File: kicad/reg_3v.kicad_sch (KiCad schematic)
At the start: 7 parts

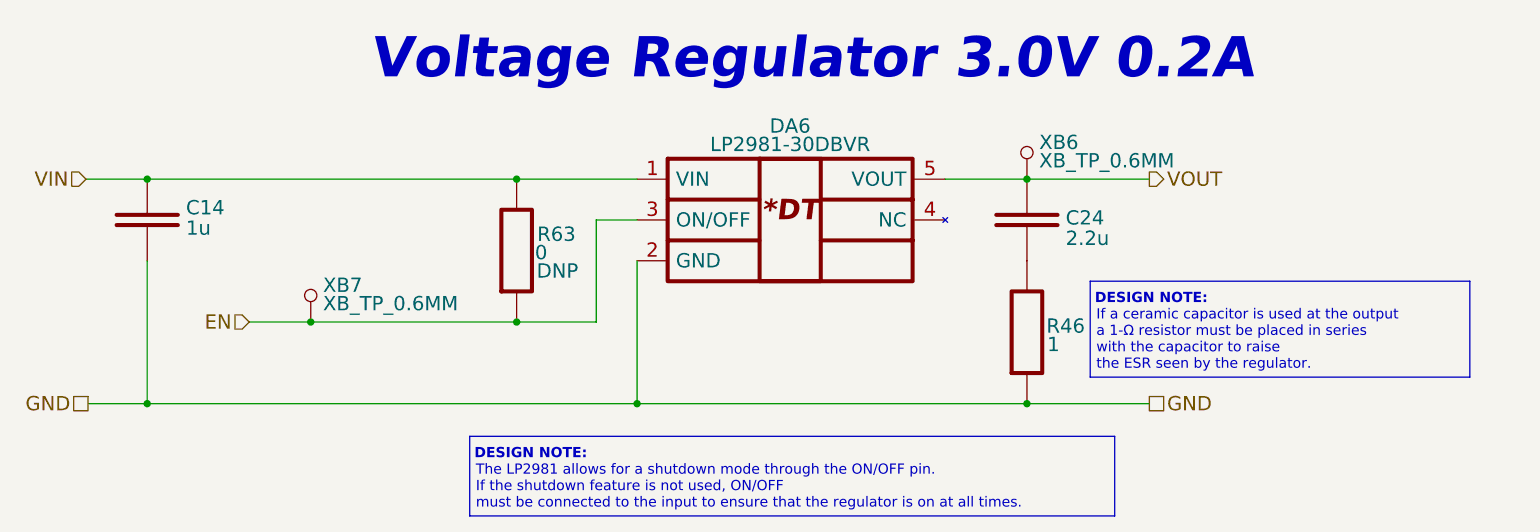
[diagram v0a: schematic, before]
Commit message: Reannotate schematic; Fix 5032 crystal footprint field; Update PCB with 5032 crystal
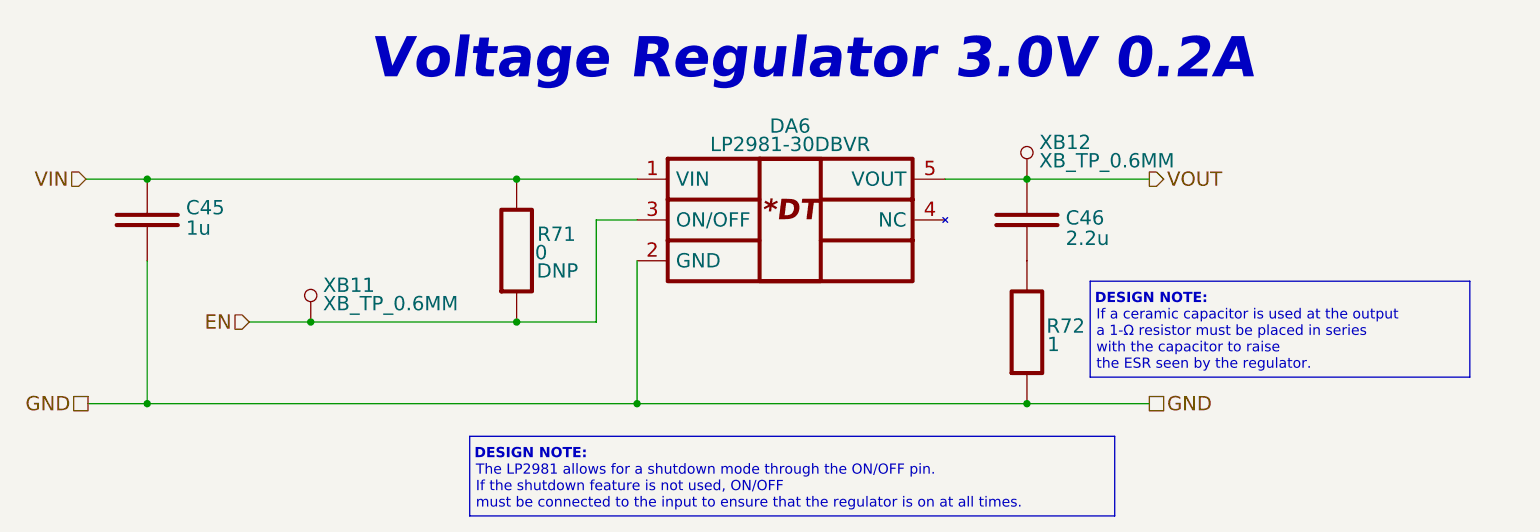
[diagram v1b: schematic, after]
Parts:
- renumbered C14 to C45, C24 to C46, R63 to R71, R46 to R72, XB7 to XB11, XB6 to XB12
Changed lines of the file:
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@@
   (symbol (lib_id "Capacitors:C_CAP") (at 183.642 85.598 270) (mirror x) (unit 1)
     (in_bom yes) (on_board yes)
-    (property "Reference" "C24" (id 0) (at 188.468 85.344 90)
+    (property "Reference" "C46" (id 0) (at 188.468 85.344 90)
       (effects (font (size 1.778 1.778)) (justify left))
     )
@@
   (symbol (lib_id "Capacitors:C_CAP") (at 74.168 85.598 270) (unit 1)
     (in_bom yes) (on_board yes)
-    (property "Reference" "C14" (id 0) (at 78.994 84.074 90)
+    (property "Reference" "C45" (id 0) (at 78.994 84.074 90)
       (effects (font (size 1.778 1.778)) (justify left))
     )
@@
   (symbol (lib_id "Connectors:XB_TP_0.6MM") (at 94.5147 98.298 0) (unit 1)
     (in_bom no) (on_board yes)
-    (property "Reference" "XB7" (id 0) (at 96.0387 93.726 0)
+    (property "Reference" "XB11" (id 0) (at 96.0387 93.726 0)
       (effects (font (size 1.778 1.778)) (justify left))
     )
@@
   (symbol (lib_id "Connectors:XB_TP_0.6MM") (at 183.642 80.518 0) (unit 1)
     (in_bom no) (on_board yes)
-    (property "Reference" "XB6" (id 0) (at 185.166 75.946 0)
+    (property "Reference" "XB12" (id 0) (at 185.166 75.946 0)
       (effects (font (size 1.778 1.778)) (justify left))
     )
@@
   (symbol (lib_id "Resistors:R_RES") (at 183.642 99.568 90) (unit 1)
     (in_bom yes) (on_board yes)
-    (property "Reference" "R46" (id 0) (at 188.468 98.806 90)
+    (property "Reference" "R72" (id 0) (at 188.468 98.806 90)
       (effects (font (size 1.778 1.778)))
     )
@@
   (symbol (lib_id "Resistors:R_RES") (at 120.142 89.408 90) (unit 1)
     (in_bom yes) (on_board yes)
-    (property "Reference" "R63" (id 0) (at 125.095 87.376 90)
+    (property "Reference" "R71" (id 0) (at 125.095 87.376 90)
       (effects (font (size 1.778 1.778)))
     )

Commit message: Add voltage value to caps, update BOM, SCH, ASM
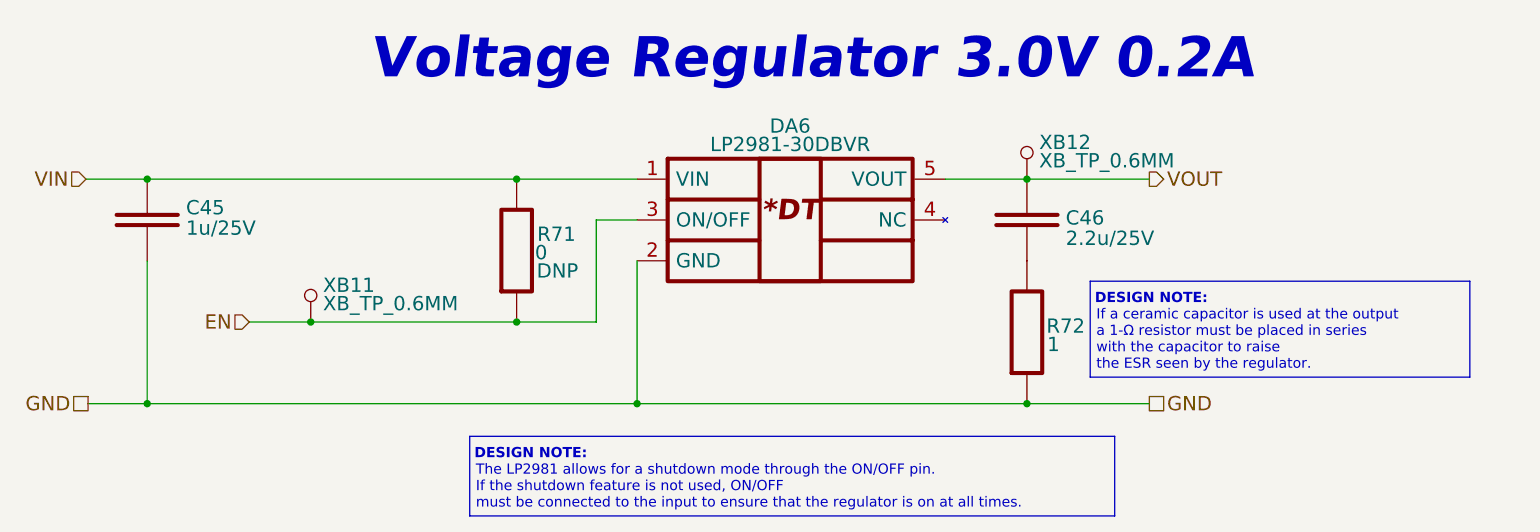
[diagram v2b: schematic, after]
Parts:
- C45: value 1u -> 1u/25V; Case/Package (none) -> 0603; Tolerance (none) -> ±10%; Type (none) -> X7R
- C46: value 2.2u -> 2.2u/25V; Case/Package (none) -> 0603; Tolerance (none) -> ±10%; Type (none) -> X7R
- R71: Case/Package 0000 -> 0603; Tolerance ±% -> ±5%
- R72: Tolerance ±% -> ±5%
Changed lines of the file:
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@@
     (effects (font (size 1.778 1.778)) (justify left))
   )
-  (symbol (lib_id "Capacitors:C_CAP") (at 183.642 85.598 270) (mirror x) (unit 1)
+  (symbol (lib_name "C_CAP_1") (lib_id "Capacitors:C_CAP") (at 183.642 85.598 270) (mirror x) (unit 1)
     (in_bom yes) (on_board yes)
     (property "Reference" "C46" (id 0) (at 188.468 85.344 90)
       (effects (font (size 1.778 1.778)) (justify left))
     )
-    (property "Value" "2.2u" (id 1) (at 188.468 87.884 90)
+    (property "Value" "2.2u/25V" (id 1) (at 188.468 87.884 90)
       (effects (font (size 1.778 1.778)) (justify left))
     )
@@
       (effects (font (size 1.778 1.778)))
     )
+    (property "Voltage" "" (id 5) (at 183.642 85.598 0)
+      (effects (font (size 1.27 1.27)) hide)
+    )
+    (property "Case/Package" "0603" (id 6) (at 183.642 85.598 0)
+      (effects (font (size 1.27 1.27)) hide)
+    )
+    (property "Type" "X7R" (id 7) (at 173.482 85.598 0)
+      (effects (font (size 1.27 1.27)) hide)
+    )
+    (property "Tolerance" "±10%" (id 8) (at 170.942 85.598 0)
+      (effects (font (size 1.27 1.27)) hide)
+    )
     (pin "1")
     (pin "2")
@@
       (effects (font (size 1.778 1.778)) (justify left))
     )
-    (property "Value" "1u" (id 1) (at 78.994 86.614 90)
+    (property "Value" "1u/25V" (id 1) (at 78.994 86.614 90)
       (effects (font (size 1.778 1.778)) (justify left))
     )
@@
     (property "Assembly" "" (id 4) (at 65.278 85.598 0)
       (effects (font (size 1.778 1.778)))
+    )
+    (property "Voltage" "" (id 5) (at 74.168 85.598 0)
+      (effects (font (size 1.27 1.27)) hide)
+    )
+    (property "Case/Package" "0603" (id 6) (at 74.168 85.598 0)
+      (effects (font (size 1.27 1.27)) hide)
+    )
+    (property "Type" "X7R" (id 7) (at 64.008 85.598 0)
+      (effects (font (size 1.27 1.27)) hide)
+    )
+    (property "Tolerance" "±10%" (id 8) (at 61.468 85.598 0)
+      (effects (font (size 1.27 1.27)) hide)
     )
     (pin "1")
@@
     (pin "1")
   )
-  (symbol (lib_id "Resistors:R_RES") (at 183.642 99.568 90) (unit 1)
+  (symbol (lib_name "R_RES_1") (lib_id "Resistors:R_RES") (at 183.642 99.568 90) (unit 1)
     (in_bom yes) (on_board yes)
     (property "Reference" "R72" (id 0) (at 188.468 98.806 90)
@@
       (effects (font (size 1.27 1.27)) hide)
     )
-    (property "Tolerance" "±%" (id 7) (at 193.294 99.568 0)
+    (property "Tolerance" "±5%" (id 7) (at 193.294 99.568 0)
       (effects (font (size 1.27 1.27)) hide)
     )
+    (property "Part Number" "" (id 8) (at 183.642 99.568 0))
     (pin "1")
     (pin "2")
@@
       (effects (font (size 1.778 1.778)))
     )
-    (property "Case/Package" "0000" (id 5) (at 126.492 89.408 0)
+    (property "Case/Package" "0603" (id 5) (at 126.492 89.408 0)
       (effects (font (size 1.27 1.27)) hide)
     )
@@
       (effects (font (size 1.27 1.27)) hide)
     )
-    (property "Tolerance" "±%" (id 7) (at 129.794 89.408 0)
+    (property "Tolerance" "±5%" (id 7) (at 129.794 89.408 0)
       (effects (font (size 1.27 1.27)) hide)
     )
+    (property "Part Number" "" (id 8) (at 120.142 89.408 0))
     (pin "1")
     (pin "2")

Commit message: Add wiring diagram; Add work ours (stage 2); refactor folders
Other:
- title: (none) -> RadioSens v1
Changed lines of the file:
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@@
 (kicad_sch (version 20211123) (generator eeschema)
   (paper "A4")
+  (title_block
+    (title "RadioSens v1")
+    (comment 2 "Electrical Circuit")
+  )
   (junction (at 74.168 80.518) (diameter 0) (color 0 0 0 0)
   )
